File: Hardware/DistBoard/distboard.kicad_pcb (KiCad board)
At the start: 2 copper layers, 73.4 x 47.8 mm, 10 parts, among them J1 POWER_IN, J2 FAN_HEADER, J3 PI_POWER, J4 CAN_1, J5 CAN_PI, J6 CAN_2, J7 CAN_3, J8 CAN_4, U1 MINI-360

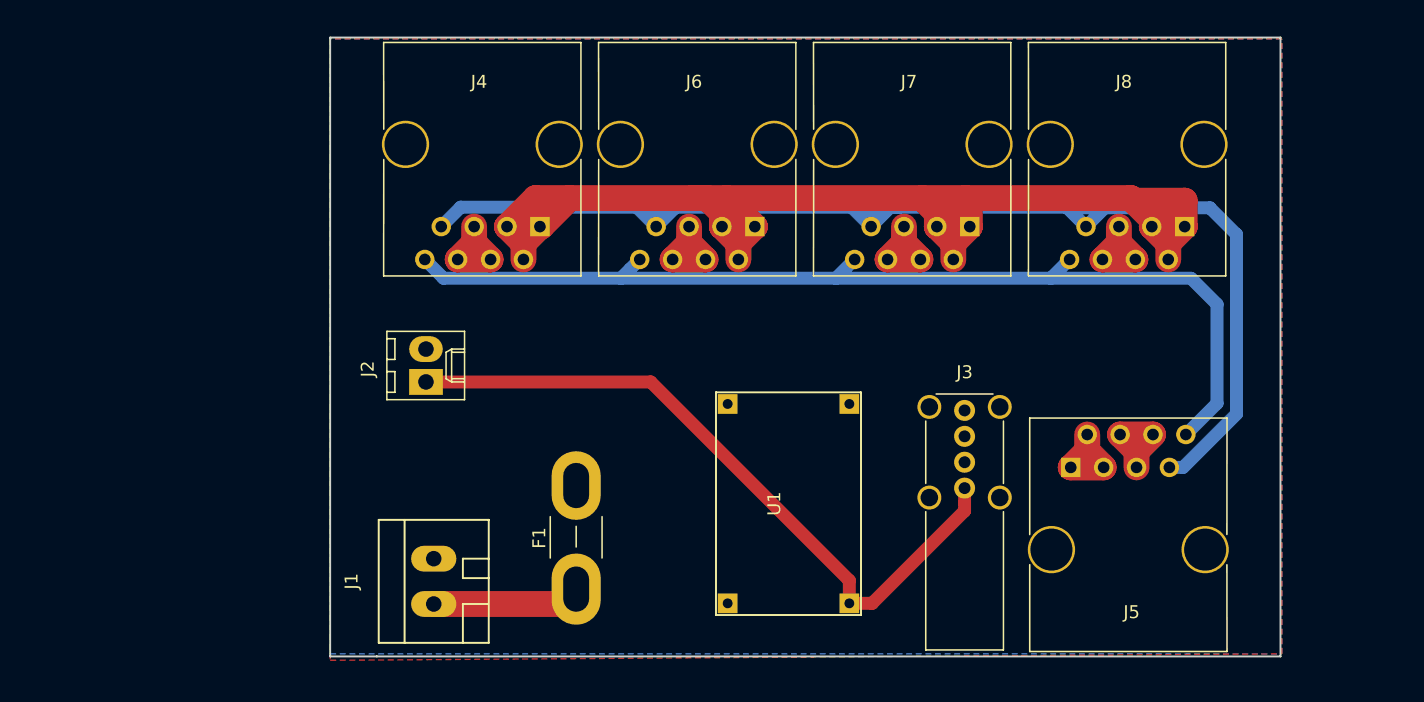
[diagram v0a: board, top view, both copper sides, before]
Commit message: Working on dist board
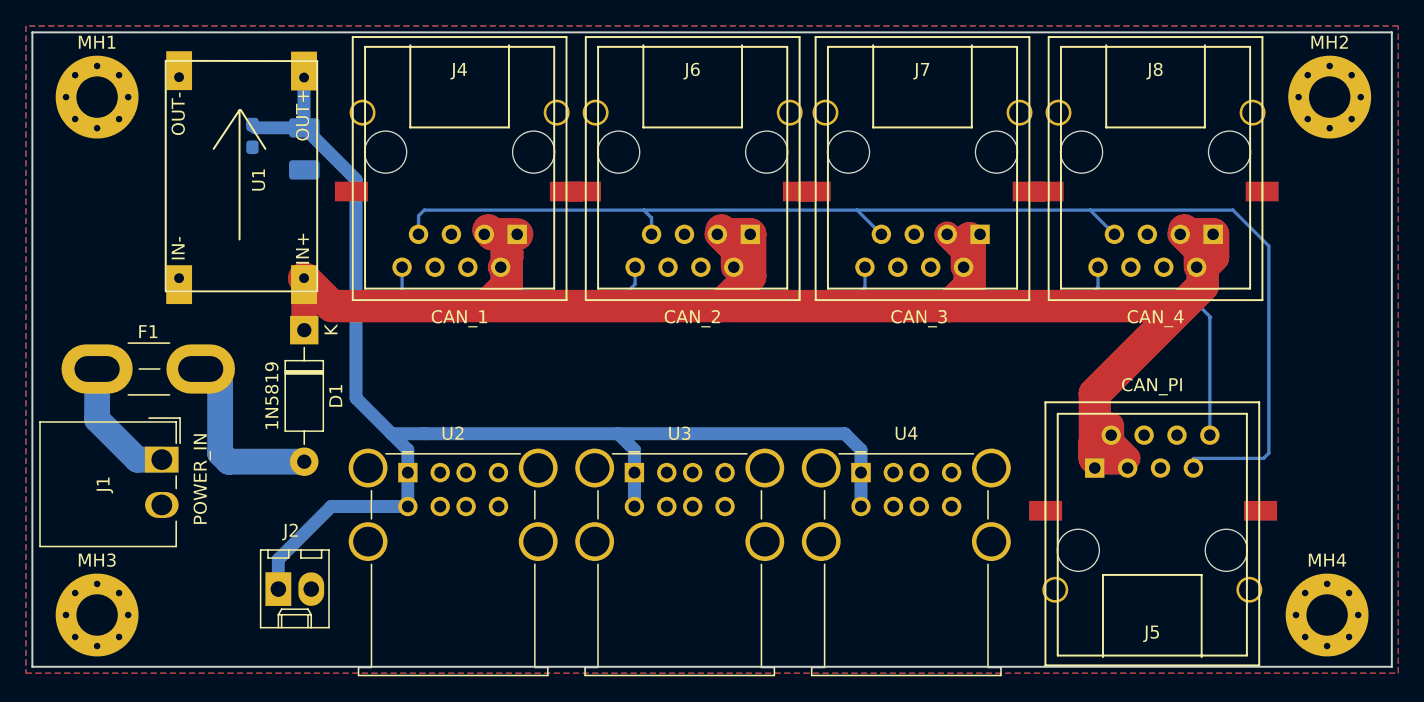
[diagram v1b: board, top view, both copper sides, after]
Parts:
- removed J3: PI_POWER, Connectors:USB_A_Vertical
- added C1: 100uF, Capacitor_Tantalum_SMD:CP_EIA-3528-21_Kemet-B_Pad1.50x2.35mm_HandSolder, B.Cu at (101.0, 39.0)
- added C2: 10uF, Capacitor_SMD:C_0603_1608Metric_Pad1.05x0.95mm_HandSolder, B.Cu at (97.0, 38.0)
- added D1: 1N5819, Diode_THT:D_DO-41_SOD81_P10.16mm_Horizontal, F.Cu at (101.0, 53.0)
- added MH1: MountingHole_Pad, MountingHole:MountingHole_3.2mm_M3_Pad_Via, F.Cu at (85.0, 35.0)
- added MH2: MountingHole_Pad, MountingHole:MountingHole_3.2mm_M3_Pad_Via, F.Cu at (180.2, 35.0)
- added MH3: MountingHole_Pad, MountingHole:MountingHole_3.2mm_M3_Pad_Via, F.Cu at (85.0, 75.0)
- added MH4: MountingHole_Pad, MountingHole:MountingHole_3.2mm_M3_Pad_Via, F.Cu at (180.0, 75.0)
- added U2: double_usb, Connector_USB:USB_A_Wuerth_61400826021_Horizontal_Stacked, F.Cu at (109.0, 64.0)
- added U3: double_usb, Connector_USB:USB_A_Wuerth_61400826021_Horizontal_Stacked, F.Cu at (126.5, 64.0)
- added U4: double_usb, Connector_USB:USB_A_Wuerth_61400826021_Horizontal_Stacked, F.Cu at (144.0, 64.0)
- J1: footprint Connectors_WAGO:WAGO_734_2pin_Straight_RuggedPads -> Connector_Wago:Wago_734-162_1x02_P3.50mm_Horizontal
- J4, J5, J6, J7, J8: footprint Connectors:RJ45_8 -> RJ45:RJ45_GENERIC
- moved F1 40.7 mm to (85.0, 56.0), turned to 0 degrees
- moved U1 31.8 mm to (102.0, 50.0), turned to 90 degrees
- moved J1 23.0 mm to (90.0, 63.0), turned to 270 degrees
- moved J2 19.6 mm to (99.0, 73.0), turned to 0 degrees
- moved J5 8.98 mm to (166.5, 70.0)
- moved J4 8.46 mm to (113.0, 39.2)
- moved J6 7.49 mm to (131.0, 39.2)
- moved J7 6.81 mm to (148.8, 39.2)
- moved J8 6.17 mm to (166.8, 39.2)
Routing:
- net +5V: track 54.4 -> 101.8 mm
- net CANGND: track 37.0 -> 0.00 mm
- net CANV: track 118.9 -> 138.5 mm
- net Net-(D1-Pad2): track 0.00 -> 14.3 mm
- net CANH: track 100.2 -> 97.9 mm
- net CANL: track 79.9 -> 81.7 mm
- net Net-(F1-Pad1): track 11.5 -> 10.2 mm
- added copper zone on F.Cu, net CANGND
- removed copper zone on F.Cu, net CANV
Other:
- board size 73.4 x 47.8 mm -> 105 x 49 mm
- net class 5V added: clearance 0.2, trace_width 1, via_dia 0.8, via_drill 0.4
- net class CANGND added: clearance 0.2, trace_width 2, via_dia 0.8, via_drill 0.4
- net class CANV: clearance 1 -> 0.5; trace_width 1 -> 2

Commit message: Finished distboard design
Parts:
- added D2: POWER, LED_SMD:LED_0805_2012Metric_Pad1.15x1.40mm_HandSolder, F.Cu at (94.1, 75.7)
- added R1: 1K, Resistor_SMD:R_0603_1608Metric_Pad1.05x0.95mm_HandSolder, F.Cu at (93.0, 72.7)
- added shm_logo_small: , shm_logo:shm_logo_small, F.Cu at (80.8, 51.5)
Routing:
- net +5V: track 101.8 -> 106.8 mm
- net Net-(D2-Pad1): track 0.00 -> 2.15 mm
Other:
- board text added: "Dome DistBoard v0.1b JagDev"
